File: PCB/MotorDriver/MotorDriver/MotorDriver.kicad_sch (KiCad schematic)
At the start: 75 parts, among them J13 JST-XH, J14 JST-XH, J2 JST-XH, J3 XT30PW-M, J5 JST-XH, J6 JST-XH, J7 JST-XH, J8 JST-XH, J9 JST-XH, Q10 NMOS, Q3 TJ60S04M3L, SW1 SW_Push, SW2 SW_DPST_x2, U1 Pico, U15 AZ1117CH-3.3TR, U3 TCA9548APWR

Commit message: ✏️ 昔のファイルを引っ張てきた
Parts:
- removed D9: ＧＳ１０１０ＦＬ, Diode_SMD:D_SOD-123F, symbol Device:D
- Q10: footprint TPH11006NL:TPH11006NL_SOP Advance_TOS-M -> Package_TO_SOT_SMD:SOT-23
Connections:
- net GND: no longer R5.2
- net at Q3.1 (G), SW2.1 (A): now also R5.2
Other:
- moved on the sheet: C25, C26, C8, D20, D9, SW2A, U15

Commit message: :sparkles: Production Done
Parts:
- Q10: footprint Package_TO_SOT_SMD:SOT-23 -> TPH11006NL:TPH11006NL_SOP Advance_TOS-M
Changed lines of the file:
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@@
       (effects (font (size 1.27 1.27)) (justify left))
     )
-    (property "Footprint" "Package_TO_SOT_SMD:SOT-23" (at 154.94 86.36 0)
+    (property "Footprint" "TPH11006NL:TPH11006NL_SOP Advance_TOS-M" (at 154.94 86.36 0)
       (effects (font (size 1.27 1.27)) hide)
     )

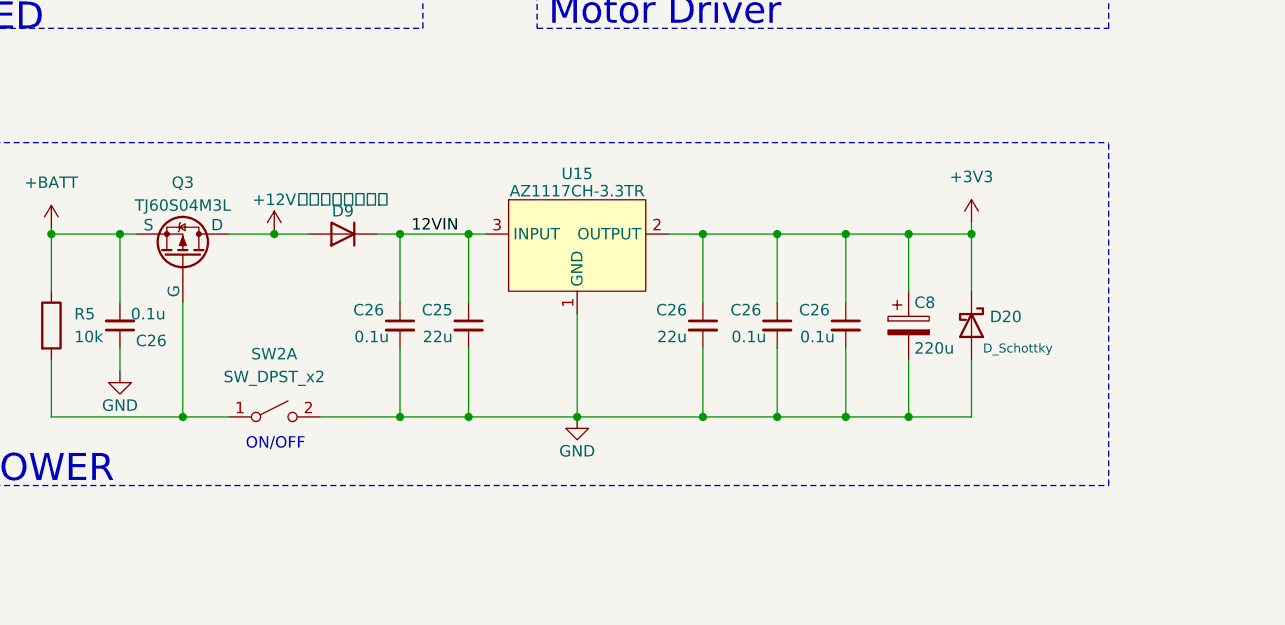
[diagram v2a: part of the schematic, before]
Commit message: ✏️ [PCB] モータからの逆起電力対策ダイオードを追加
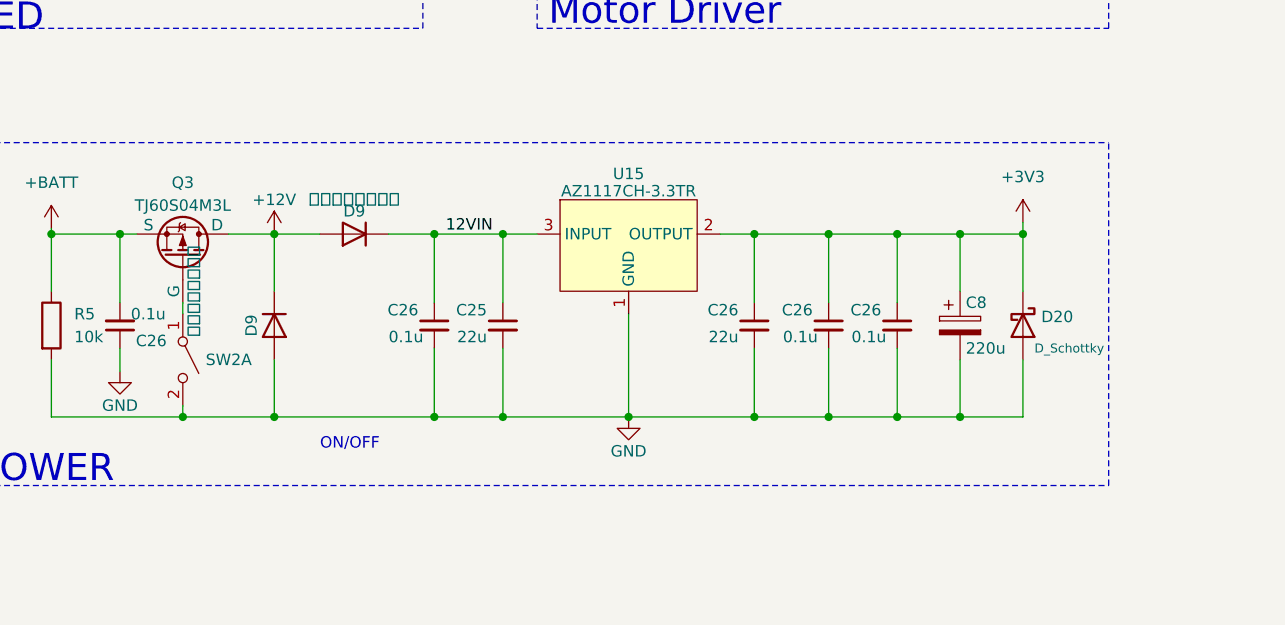
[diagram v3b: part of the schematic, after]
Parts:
- added D9: ＧＳ１０１０ＦＬ, Diode_SMD:D_SOD-123F, symbol Device:D
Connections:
- net +12V: now also D9.1 (K)
- net GND: now also R5.2, D9.2 (A)
- net at Q3.1 (G), SW2.1 (A): no longer R5.2
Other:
- moved on the sheet: C25, C26, C8, D20, D9, SW2A, U15
